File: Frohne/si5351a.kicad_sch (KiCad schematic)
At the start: 9 parts, among them J8 BNC, U4 MS5351M

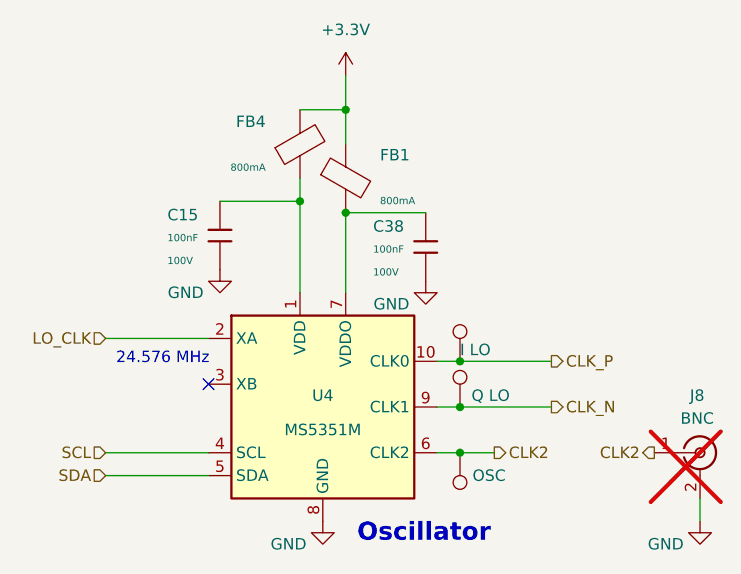
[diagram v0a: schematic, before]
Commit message: Added R37 asd R38
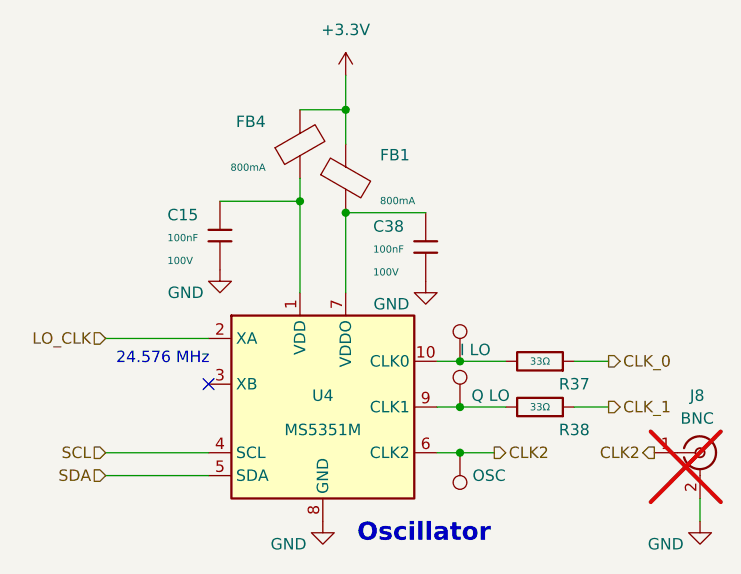
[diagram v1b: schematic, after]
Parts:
- added R37, R38: 33Ω, PCM_JLCPCB:R_0805, symbol PCM_JLCPCB-Resistors:0805,33Ω
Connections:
- net CLK_N: no longer names the net of TP4.1, U4.9 (CLK1)
- net CLK_N: now also R38.2
- net CLK_P: no longer names the net of TP3.1, U4.10 (CLK0)
- net CLK_P: now also R37.2
- new net CLK_0: R37.1
- new net CLK_1: R38.1
